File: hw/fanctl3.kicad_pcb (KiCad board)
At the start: 2 copper layers, 88.8 x 67.2 mm, 62 parts, among them P1 CONN_01X03, P2 CONN_02X05, P3 MOLEX_PWR, P4 CONN_01X04, Q1 FAN_NMOS, Q2 FAN_NMOS, Q3 FAN_NMOS, Q4 FAN_NMOS, Q5 FAN_NMOS, Q6 FAN_NMOS, U1 4051, U2 P82B96, Y1 Crystal_Small

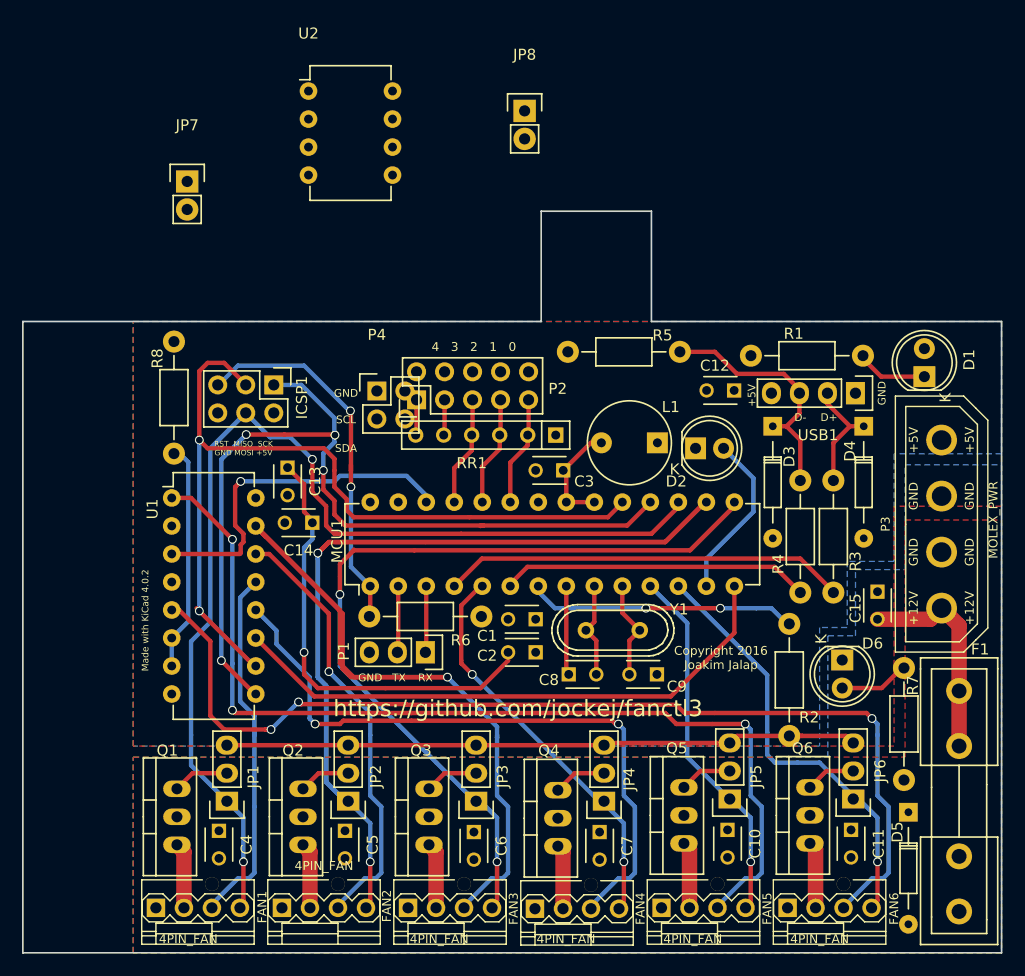
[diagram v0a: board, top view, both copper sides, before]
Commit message: Add i2c port and a resistor for the LED.
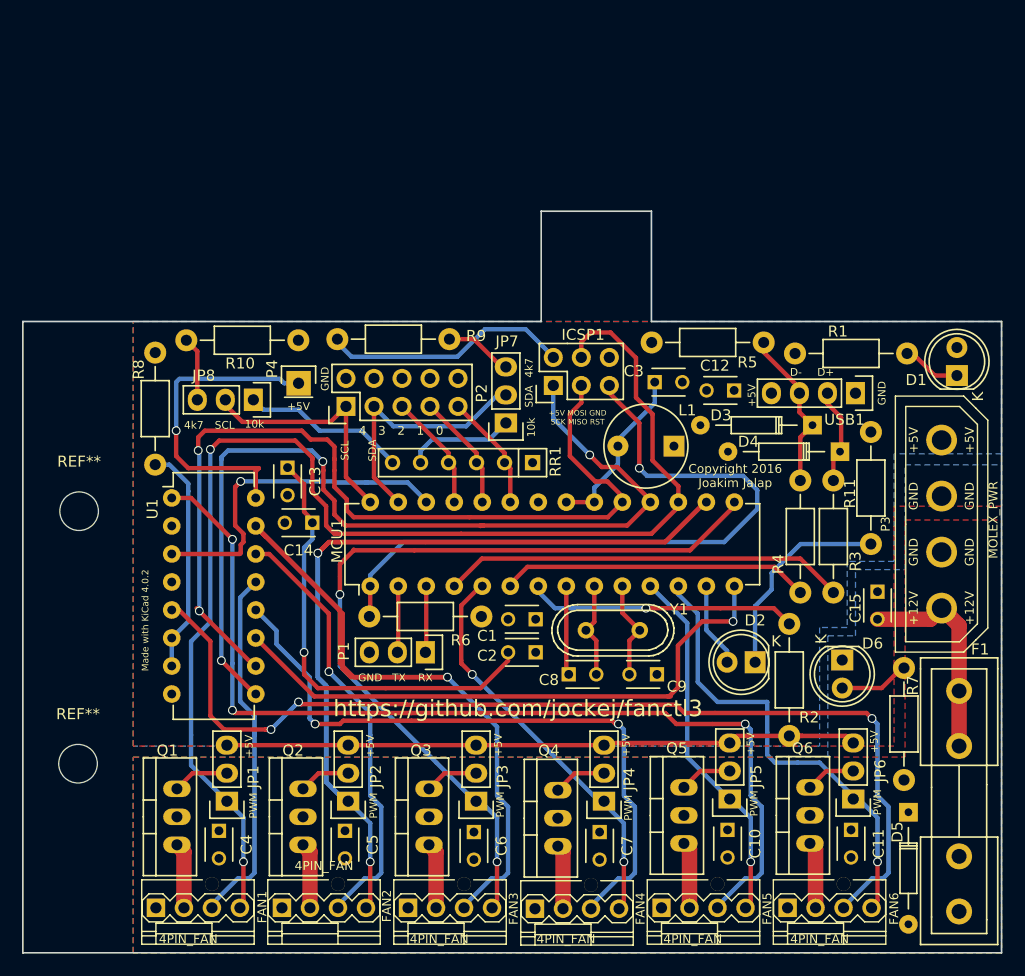
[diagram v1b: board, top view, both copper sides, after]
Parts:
- removed U2: P82B96, Housings_DIP:DIP-8_W7.62mm
- added R10: 4k7, Resistors_ThroughHole:Resistor_Horizontal_RM10mm, F.Cu at (83.4, 102.2)
- added R11: R, Resistors_ThroughHole:Resistor_Horizontal_RM10mm, F.Cu at (140.4, 115.6)
- added R9: 4k7, Resistors_ThroughHole:Resistor_Horizontal_RM10mm, F.Cu at (97.1, 102.1)
- added REF**: MountingHole_3-5mm, Mounting_Holes:MountingHole_3-5mm, F.Cu at (68.6, 117.7)
- added REF**: MountingHole_3-5mm, Mounting_Holes:MountingHole_3-5mm, F.Cu at (68.5, 140.6)
- JP7, JP8: value Jumper_NC_Small -> JUMPER3; footprint Pin_Headers:Pin_Header_Straight_1x02 -> Pin_Headers:Pin_Header_Straight_1x03
- P4: value CONN_01X04 -> CONN_01X01; footprint Pin_Headers:Pin_Header_Straight_2x02 -> Pin_Headers:Pin_Header_Straight_1x01
- RR1: value RR5 -> 10k
- moved JP7 36.3 mm to (107.3, 109.7), turned to 180 degrees
- moved JP8 35.9 mm to (84.4, 107.6), turned to 270 degrees
- moved ICSP1 25.4 mm to (111.6, 106.3), turned to 90 degrees
- moved D2 20.1 mm to (129.9, 131.4), turned to 180 degrees
- moved C3 11.5 mm to (120.8, 106.0), turned to 0 degrees
- moved R5 7.65 mm to (125.6, 102.4)
- moved P4 7.13 mm to (88.5, 106.1)
- moved P2 6.43 mm to (92.8, 108.2)
- moved R1 4.00 mm to (138.6, 103.4)
- moved D3 3.60 mm to (135.1, 109.9), turned to 180 degrees
- moved RR1 3.26 mm to (102.1, 113.3)
- moved D4 3.15 mm to (137.6, 112.3), turned to 180 degrees
- moved D1 2.95 mm to (148.2, 105.4)
- moved R8 1.97 mm to (75.5, 108.4)
- moved L1 1.53 mm to (120.0, 111.8)
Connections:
- D2 pad 1: GND -> Net-(D2-Pad1)
- P2 pad 1: Net-(JP8-Pad1) -> TEMP4/SCL
- P2 pad 3: Net-(JP7-Pad1) -> TEMP3/SDA
- P4 pad 1: Net-(P4-Pad1) -> +5V
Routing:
- net +5V: track 24.3 -> 75.9 mm
- net Net-(ICSP1-Pad5): track 34.4 -> 63.2 mm, vias 2 -> 1
- net TEMP3/SDA: track 0.02 -> 23.5 mm
- net TEMP4/SCL: track 0.28 -> 22.5 mm
- net PWM0: track 97.5 -> 117.7 mm
- net Net-(D2-Pad1): track 0.00 -> 18.8 mm
- net Net-(JP8-Pad1): track 3.23 -> 15.0 mm
- net Net-(D3-Pad1): track 22.8 -> 15.1 mm
- net Net-(D2-Pad2): track 15.4 -> 7.90 mm
- net Net-(JP7-Pad1): track 3.23 -> 9.85 mm
- net Net-(JP7-Pad3): track 0.00 -> 6.16 mm
- net Net-(JP8-Pad3): track 0.00 -> 5.81 mm
- net Net-(C3-Pad1): track 10.0 -> 15.7 mm
- net SEL1: track 78.6 -> 82.4 mm
- net SEL2: track 80.5 -> 83.2 mm, vias 4 -> 3
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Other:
- board text added: "+5V MOSI GND SCK MISO RST"
- board text added: "10k"
- board text added: "4k7"
- board text added: "PWM"
- board text removed: "RST MISO SCK GND MOSI +5V"
